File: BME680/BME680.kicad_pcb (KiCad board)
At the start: 2 copper layers, 25.4 x 17.8 mm, 28 parts, among them J1 Conn_01x06, J2 Conn_01x04, J3 Conn_01x06, J4 Conn_01x04, Q1 BSS138DW, Q2 BSS138DW, U1 AP2127K-3.3, U2 BME680

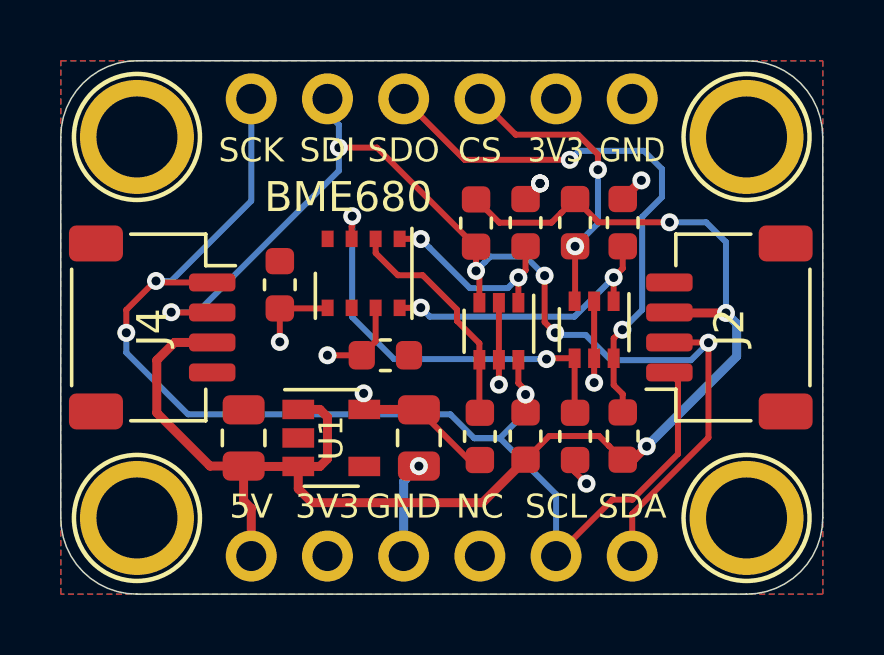
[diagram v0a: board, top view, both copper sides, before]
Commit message: Copper Pour Edits
Copper pour reduced to have 0.2mm edge clearance
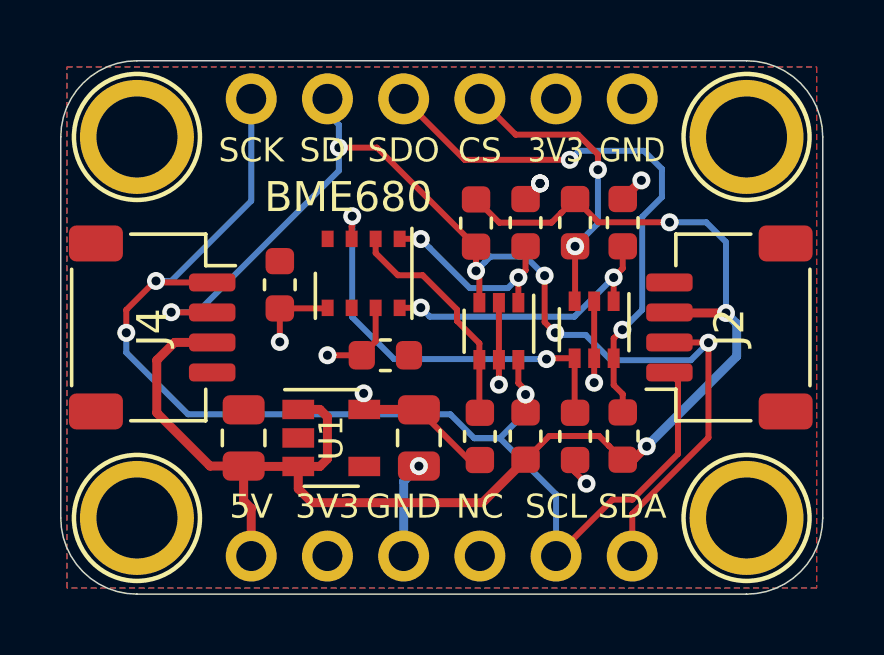
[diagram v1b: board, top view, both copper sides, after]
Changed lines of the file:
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@@
     (polygon
       (pts
-        (xy 52.578 27.0764) (xy 77.978 27.0764) (xy 77.978 44.8564) (xy 52.578 44.8564)
+        (xy 52.7812 27.2796) (xy 77.7748 27.2796) (xy 77.7748 44.6532) (xy 52.7812 44.6532)
       )
     )
@@
     (polygon
       (pts
-        (xy 52.578 27.0764) (xy 77.978 27.0764) (xy 77.978 44.8564) (xy 52.578 44.8564)
+        (xy 52.7812 27.2796) (xy 77.7748 27.2796) (xy 77.7748 44.6532) (xy 52.7812 44.6532)
       )
     )

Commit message: Silkscreen Edit
VOC and Temperature swopped around
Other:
- board text added: "VOC's Temperature"
- board text removed: "Temperature VOCs"

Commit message: Soldermask width adjusted
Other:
- rule solder_mask_min_width: 0.1 -> 0.05
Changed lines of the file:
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@@
     (pad_drill 1)
     (pad_to_mask_clearance 0)
-    (solder_mask_min_width 0.1)
+    (solder_mask_min_width 0.05)
     (aux_axis_origin 0 0)
     (visible_elements 7FFFFFFF)
